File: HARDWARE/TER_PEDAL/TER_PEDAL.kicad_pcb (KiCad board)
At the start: 4 copper layers, 78.6 x 34.5 mm, 60 parts, among them J1 DEBUG, J2 APPS_1, J3 RJ45_Shielded, J4 APPS_2, J5 BPPS_1, J6 SteerSensor, SW1 RST, U1 STM32F103C8Tx, U2 TSR_1-2450, U3 LM1117MP-3.3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

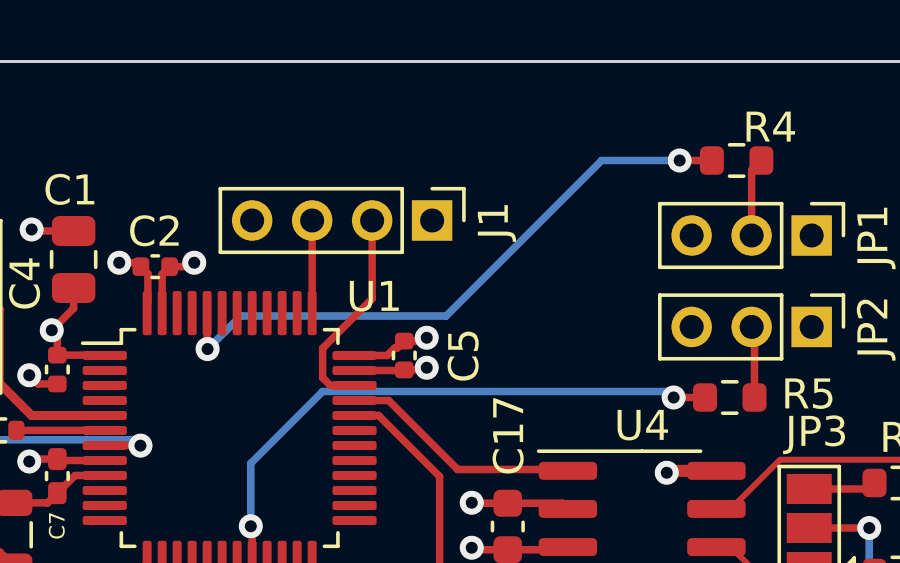
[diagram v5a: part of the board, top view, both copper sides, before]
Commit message: Quick Fix on the debug conector Bus where it was not connected to 3.3V + Labels
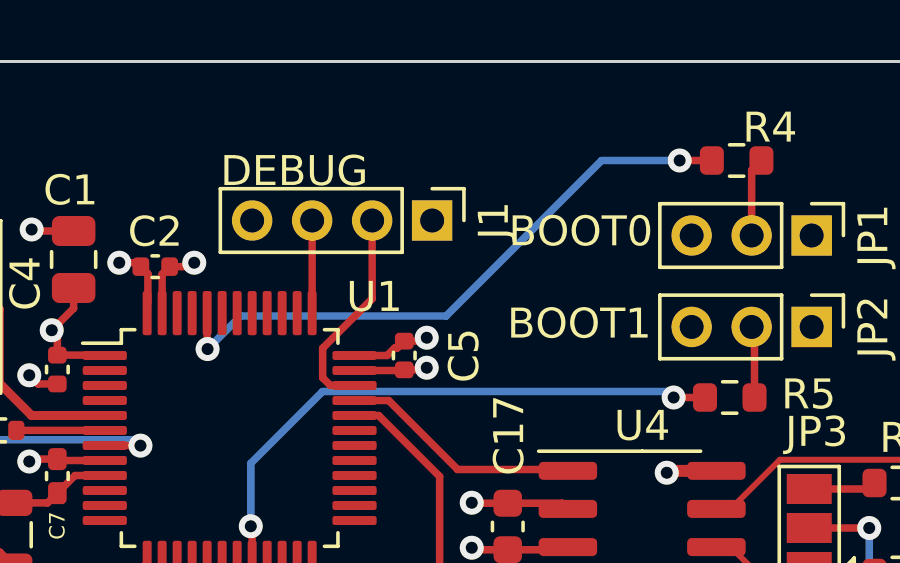
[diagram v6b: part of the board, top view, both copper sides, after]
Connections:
- J1 pad 4: +3V3 -> +3.3V
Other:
- board text added: "BOOT0"
- board text added: "BOOT1"
- board text added: "DEBUG"

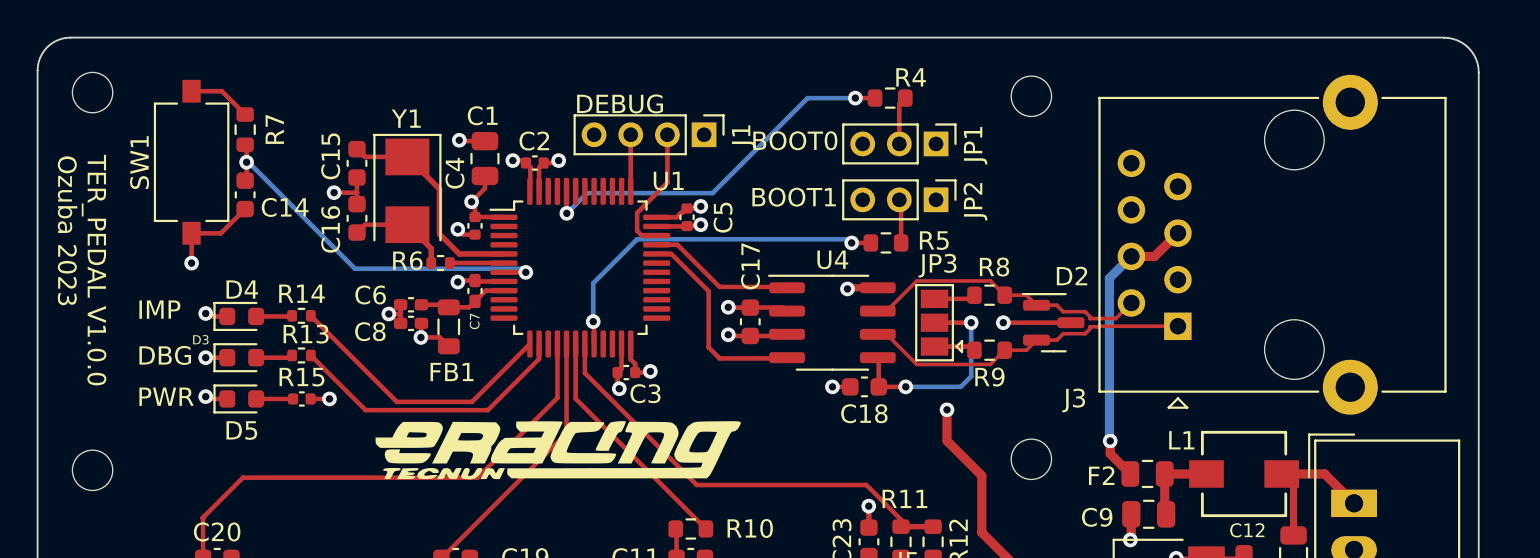
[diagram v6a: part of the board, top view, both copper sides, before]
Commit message: Bumped Bugfix version and fixed unnecessary BOOT0 pin and rj45 placement
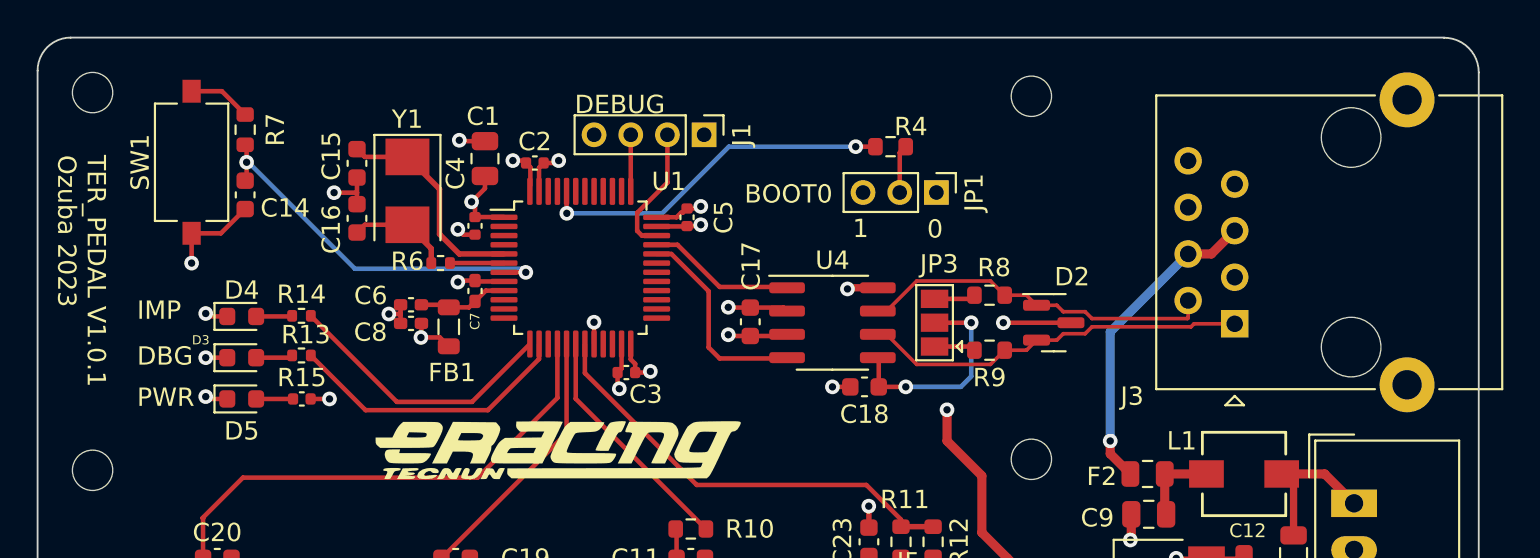
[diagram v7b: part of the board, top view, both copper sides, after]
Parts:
- removed JP2: BOOT1, Connector_PinHeader_2.00mm:PinHeader_1x03_P2.00mm_Vertical
- removed R5: 10k, Resistor_SMD:R_0603_1608Metric
- moved J3 3.10 mm to (176.7, 91.8)
- moved JP1 2.65 mm to (160.4, 84.7)
- moved R4 2.65 mm to (157.9, 82.2)
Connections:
- U1 pad 20: /MICRO/BOOT1 -> GND
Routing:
- net /MICRO/BOOT1: track 19.6 -> 0.00 mm, vias 2 -> 0
- net /CAN/CAN+: track 15.8 -> 19.4 mm
- net /CAN/CAN-: track 18.0 -> 21.1 mm
- net Net-(JP2-C): track 2.39 -> 0.00 mm
- net +24V: track 15.9 -> 17.3 mm
- net GND: track 55.8 -> 57.0 mm, vias 20 -> 21
- net /MICRO/BOOT0: track 20.6 -> 19.5 mm
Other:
- board text added: "0"
- board text added: "1"
- board text added: "TER_PEDAL V1.0.1 Ozuba 2023"
- board text removed: "BOOT1"
- board text removed: "TER_PEDAL V1.0.0 Ozuba 2023"
